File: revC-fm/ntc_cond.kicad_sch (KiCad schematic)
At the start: 6 parts, among them U35 LT6004CMS8#PBF

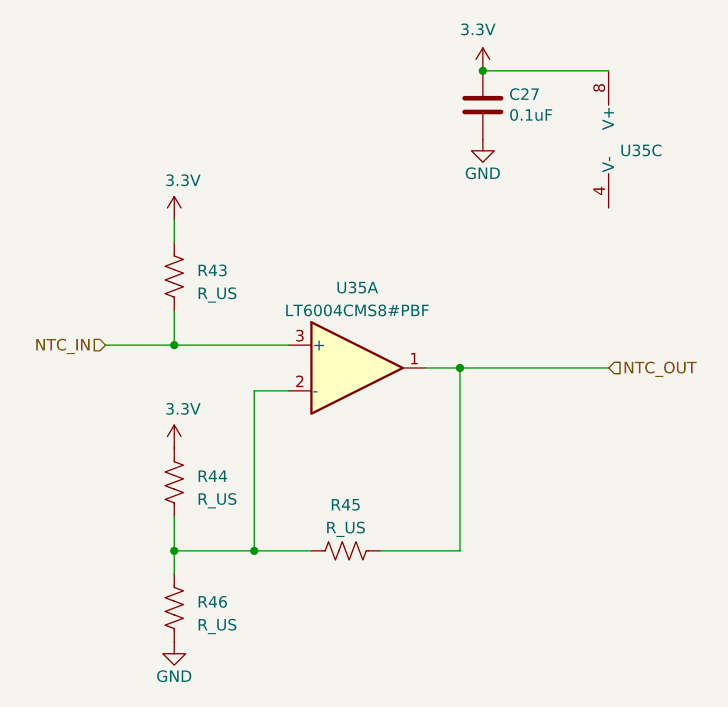
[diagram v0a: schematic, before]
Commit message: updated analog , solar comp, layout
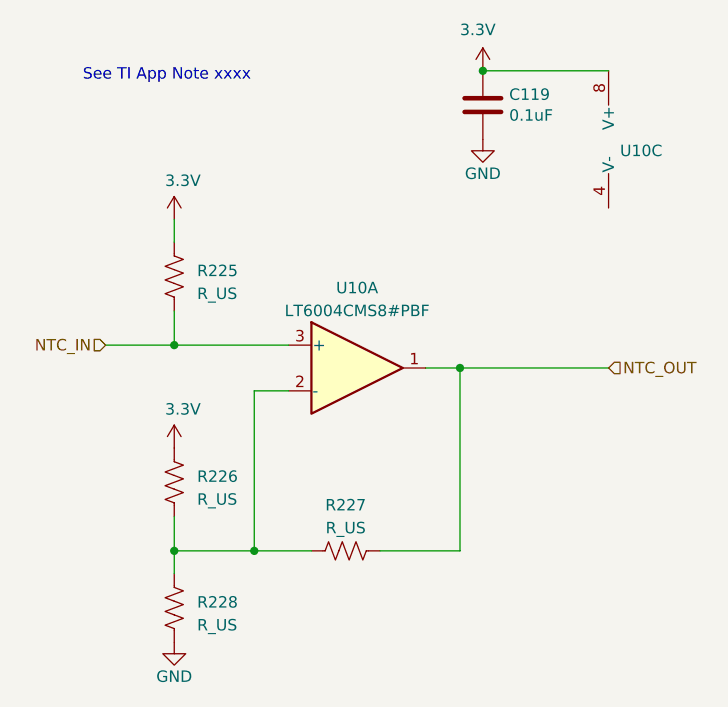
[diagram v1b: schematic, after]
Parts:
- renumbered C27 to C119, R43 to R225, R44 to R226, R45 to R227, R46 to R228, U35 to U10
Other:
- note added: "See TI App Note xxxx"
